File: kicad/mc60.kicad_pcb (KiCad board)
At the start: 2 copper layers, 60 x 70 mm, 107 parts, among them CN1 Conn_GPS, CN2 Conn_GNSS, CN3 SD_CARD, CN4 SIM_Card, CN5 Audio-Jack-4, CN6 5V_IN, J1 B_LS_N, J2 B_VRTC, J3 B_SPKP, J4 B_SPKN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

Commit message: layout WIP
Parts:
- H4: value ON_OFF -> ON<>OFF
- moved G3 57.7 mm to (121.5, 75.0)
- moved D3 18.1 mm to (98.5, 120.0), turned to 0 degrees
- moved R9 14.5 mm to (98.5, 118.0)
- moved R8 13.0 mm to (125.3, 75.8)
- moved Q1 12.9 mm to (123.0, 76.0), turned to 90 degrees
- moved D2 12.8 mm to (127.1, 76.0)
- moved Q2 10.8 mm to (98.5, 115.5), turned to 270 degrees
- moved R14 9.66 mm to (116.8, 107.0), turned to 270 degrees
- moved C1 2.52 mm to (112.0, 88.2), turned to 90 degrees
- moved C17 0.90 mm to (118.2, 106.8), turned to 270 degrees
- moved C16 0.75 mm to (115.2, 106.8), turned to 270 degrees
- moved G2 0.43 mm to (119.8, 123.2)
- moved G1 0.14 mm to (125.5, 119.5)
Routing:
- net /NETLIGHT: track 18.2 -> 33.9 mm
- net /GNSSVCC: track 32.7 -> 17.3 mm, vias 2 -> 0
- net VBAT: track 144.6 -> 141.3 mm
- net /VDD_EXT: track 63.6 -> 60.3 mm
- net GNDD: track 78.6 -> 75.8 mm
- net VDD: track 141.8 -> 143.8 mm
- net GND: track 269.3 -> 271.3 mm, vias 159 -> 161
- net Net-(Q2-Pad3): track 1.25 -> 2.10 mm
- net /SD_DET>: track 42.5 -> 41.9 mm
- net Net-(D3-Pad1): track 1.45 -> 2.02 mm
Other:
- board text added: "CITA STYLE TRSS L | R | G | M"
- board text added: "GND|3V3|GND"
- board text added: "GND|TXD|RXD"
- board text added: "ON<>OFF"
- board text added: "TXD|RNG|DTR|RTS DET|RXD|DCD|CTS"
- board text added: "[-] [+]"

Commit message: layout wip
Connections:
- CN3 pad 1: Net-(CN3-Pad1) -> (no net)
- CN3 pad 2: Net-(CN3-Pad2) -> (no net)
- CN3 pad 8: Net-(CN3-Pad8) -> (no net)
- CN4 pad P6: Net-(CN4-PadP6) -> (no net)
- D1 pad 4: Net-(D1-Pad4) -> (no net)
- D1 pad 5: Net-(D1-Pad5) -> (no net)
- D4 pad 4: Net-(D4-Pad4) -> (no net)
- D4 pad 5: Net-(D4-Pad5) -> (no net)
- U1 pad 10: Net-(U1-Pad10) -> (no net)
- U1 pad 11: Net-(U1-Pad11) -> (no net)
- U1 pad 12: Net-(U1-Pad12) -> (no net)
- U1 pad 13: Net-(U1-Pad13) -> (no net)
- U1 pad 46: Net-(U1-Pad46) -> (no net)
- U1 pad 55: Net-(U1-Pad55) -> (no net)
- U1 pad 56: Net-(U1-Pad56) -> (no net)
- U1 pad 57: Net-(U1-Pad57) -> (no net)
- U1 pad 58: Net-(U1-Pad58) -> (no net)
- U1 pad 59: Net-(U1-Pad59) -> (no net)
- U1 pad 60: Net-(U1-Pad60) -> (no net)
- U1 pad 61: Net-(U1-Pad61) -> (no net)
- U1 pad 62: Net-(U1-Pad62) -> (no net)
- U1 pad 63: Net-(U1-Pad63) -> (no net)
- U1 pad 64: Net-(U1-Pad64) -> (no net)
- U1 pad 65: Net-(U1-Pad65) -> (no net)
- U1 pad 66: Net-(U1-Pad66) -> (no net)
- U1 pad 67: Net-(U1-Pad67) -> (no net)
- U1 pad 68: Net-(U1-Pad68) -> (no net)
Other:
- net class 0.70mm removed
- net class 0.72mm added: clearance 0.2, trace_width 0.69, via_dia 0.8, via_drill 0.4
- net class 0.7mmANT added: clearance 0.128, trace_width 0.7, via_dia 0.7, via_drill 0.4
- net class Default: clearance 0.2 -> 0.128
- rule trace_clearance: 0.2 -> 0.128
- rule trace_min: 0.2 -> 0.1

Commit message: layout WIP
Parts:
- added G2: KiCad, mc60_fp:KiCad-Logo2_6mm_SilkScreen_Mask, F.Cu at (119.8, 123.2)
- G1: footprint mc60_fp:Logo_silk_OSHW_6x6mm -> mc60_fp:Logo_silk_OSHW_6x6mm_mask
- moved G3 6.50 mm to (115.5, 72.5), turned to 45 degrees
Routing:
- net VDD: track 143.8 -> 153.8 mm
- net /2V8_SD: track 36.6 -> 43.9 mm
- net GND: track 271.3 -> 272.8 mm, vias 161 -> 163
- net /RIGHT: track 11.5 -> 10.1 mm
- net /MIC_P: track 44.3 -> 43.4 mm
- added copper zone on F.Cu, net (none)
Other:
- net class Default: clearance 0.128 -> 0.2
- rule trace_clearance: 0.128 -> 0.2
- board text added: "CTIA STYLE TRSS L|R|G|M"
- board text added: "WYOLUM"
- board text removed: "CITA STYLE TRSS L | R | G | M"

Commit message: layout wip
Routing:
- net GND: track 272.8 -> 274.1 mm
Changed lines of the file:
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@@
-(kicad_pcb (version 20171130) (host pcbnew 5.0.0-rc2-dev-unknown-5d71153~64~ubuntu17.10.1)
+(kicad_pcb (version 20171130) (host pcbnew 5.0.0-rc2-dev-unknown-c8a7840~64~ubuntu16.04.1)
   (general
     (thickness 1.6)
     (drawings 25)
-    (tracks 1046)
+    (tracks 1048)
     (zones 0)
     (modules 108)
@@
     (0 F.Cu signal)
     (31 B.Cu signal)
-    (32 B.Adhes user hide)
-    (33 F.Adhes user hide)
+    (32 B.Adhes user)
+    (33 F.Adhes user)
     (34 B.Paste user hide)
     (35 F.Paste user hide)
     (36 B.SilkS user)
     (37 F.SilkS user)
-    (38 B.Mask user hide)
+    (38 B.Mask user)
     (39 F.Mask user)
     (40 Dwgs.User user)
@@
       (effects (font (size 0.8 0.8) (thickness 0.12)) (justify mirror))
     )
-    (fp_text value B_LS_N (at 0 -3.5 -90) (layer B.SilkS)
+    (fp_text value B_LS_N (at 0 -3.5 90) (layer B.SilkS)
       (effects (font (size 0.8 0.8) (thickness 0.12)) (justify mirror))
     )
@@
   (via (at 92.25 112.25) (size 0.7) (drill 0.4) (layers F.Cu B.Cu) (net 1))
   (segment (start 92.25 111.5) (end 92.25 112.25) (width 0.7) (layer F.Cu) (net 1))
+  (segment (start 126.75 108.15) (end 126.6 108.3) (width 0.7) (layer F.Cu) (net 1))
+  (segment (start 126.75 107) (end 126.75 108.15) (width 0.7) (layer F.Cu) (net 1))
   (segment (start 119.15 111.73) (end 120.45 111.73) (width 0.7) (layer F.Cu) (net 2) (status 30))
   (segment (start 125.07 111.73) (end 125.075 111.725) (width 0.7) (layer F.Cu) (net 2) (status 30))

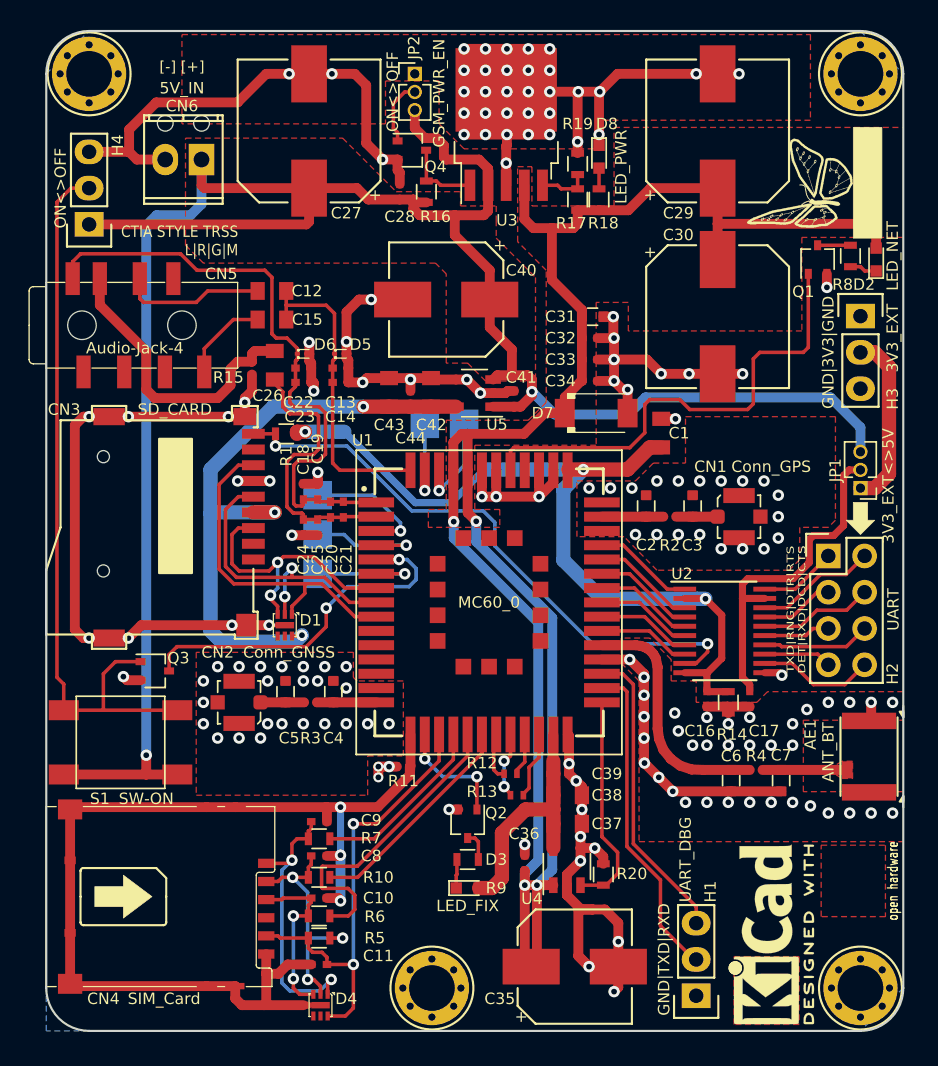
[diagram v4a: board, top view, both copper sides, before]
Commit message: UART header update, added freeite bead on Loudspeaker, added Cap for Switch
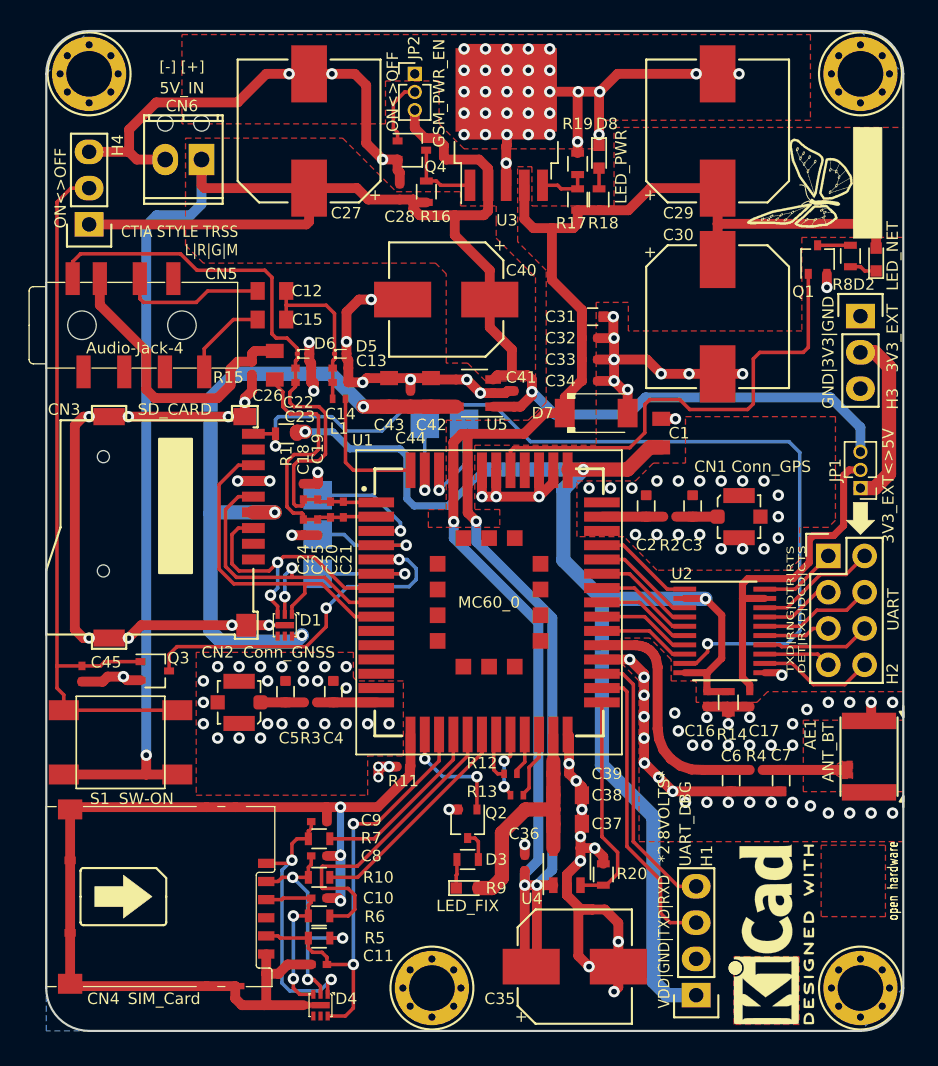
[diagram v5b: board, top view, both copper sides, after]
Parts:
- added C45: 33pF, mc60_fp:C_0402_NoSilk, F.Cu at (71.5, 105.0)
- added L1: 0E, mc60_fp:R_0402_NoSilk, F.Cu at (89.5, 85.8)
- H1: footprint mc60_fp:Pin_Header_Straight_1x03 -> mc60_fp:Pin_Header_Straight_1x04
- moved H1 2.50 mm to (114.5, 127.5)
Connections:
- C12 pad 1: /LOUD_SPKP -> /L_SP
- C13 pad 2: /LOUD_SPKP -> /L_SP
- C14 pad 2: /LOUD_SPKP -> /L_SP
- C15 pad 1: /LOUD_SPKP -> /L_SP
- D5 pad 1: /LOUD_SPKP -> /L_SP
- H1 pad 1: GND -> /VDD_EXT
- H1 pad 2: /DBG_TXD -> GND
- H1 pad 3: /DBG_RXD -> /DBG_TXD
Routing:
- net /VDD_EXT: track 60.3 -> 93.9 mm
- net /SD_DET>: track 41.9 -> 65.4 mm
- net /LOUD_SPKP: track 21.8 -> 9.23 mm
- net /L_SP: track 0.00 -> 11.7 mm
- net /2V8_SD: track 43.9 -> 48.8 mm
- net GND: track 274.1 -> 276.1 mm
- net /DBG_RXD: track 21.0 -> 19.2 mm
- net /DBG_TXD: track 22.7 -> 21.1 mm
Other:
- board text added: "*2.8VOLTS*"
- board text added: "VDD|GND|TXD|RXD"
- board text removed: "GND|TXD|RXD"

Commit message: board layout WIP
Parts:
- removed the G2 at (119.8, 123.2) (x2)
- added G2: KiCad, mc60_fp:KiCad-Logo3_6mm_SilkScreen, F.Cu at (119.8, 123.2)
- G3: footprint mc60_fp:Logo-WL3 -> mc60_fp:logo_wyo3
- S1: footprint mc60_fp:SW_SPST_DTSM -> mc60_fp:SW_SPST_WS_TASV
- moved G3 55.5 mm to (75.2, 110.8), turned to 0 degrees
- moved JP1 10.3 mm to (122.8, 82.2)
- moved C45 4.56 mm to (76.0, 105.8), turned to 270 degrees
- moved S1 4.39 mm to (72.5, 105.8)
- moved D4 2.82 mm to (90.8, 127.0), turned to 270 degrees
- moved Q3 1.69 mm to (78.0, 105.8), turned to 90 degrees
- moved JP2 1.27 mm to (94.8, 64.3)
- moved U2 1.00 mm to (117.5, 102.0)
- moved U3 0.20 mm to (101.0, 70.8)
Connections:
- CN3 pad 1: (no net) -> Net-(CN3-Pad1)
- CN3 pad 2: (no net) -> Net-(CN3-Pad2)
- CN3 pad 8: (no net) -> Net-(CN3-Pad8)
- CN4 pad P6: (no net) -> Net-(CN4-PadP6)
- D1 pad 4: (no net) -> Net-(D1-Pad4)
- D1 pad 5: (no net) -> Net-(D1-Pad5)
- D4 pad 4: (no net) -> Net-(D4-Pad4)
- D4 pad 5: (no net) -> Net-(D4-Pad5)
- SC1 pad 1: (no net) -> GND
- SC2 pad 1: (no net) -> GND
- SC3 pad 1: (no net) -> GND
- SC4 pad 1: (no net) -> GND
- U1 pad 10: (no net) -> Net-(U1-Pad10)
- U1 pad 11: (no net) -> Net-(U1-Pad11)
- U1 pad 12: (no net) -> Net-(U1-Pad12)
- U1 pad 13: (no net) -> Net-(U1-Pad13)
- U1 pad 46: (no net) -> Net-(U1-Pad46)
- U1 pad 55: (no net) -> Net-(U1-Pad55)
- U1 pad 56: (no net) -> Net-(U1-Pad56)
- U1 pad 57: (no net) -> Net-(U1-Pad57)
- U1 pad 58: (no net) -> Net-(U1-Pad58)
- U1 pad 59: (no net) -> Net-(U1-Pad59)
- U1 pad 60: (no net) -> Net-(U1-Pad60)
- U1 pad 61: (no net) -> Net-(U1-Pad61)
- U1 pad 62: (no net) -> Net-(U1-Pad62)
- U1 pad 63: (no net) -> Net-(U1-Pad63)
- U1 pad 64: (no net) -> Net-(U1-Pad64)
- U1 pad 65: (no net) -> Net-(U1-Pad65)
- U1 pad 66: (no net) -> Net-(U1-Pad66)
- U1 pad 67: (no net) -> Net-(U1-Pad67)
- U1 pad 68: (no net) -> Net-(U1-Pad68)
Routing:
- net GND: track 276.1 -> 337.2 mm, vias 163 -> 236
- net VDD: track 153.8 -> 140.6 mm
- net /VCCB: track 23.8 -> 33.4 mm
- net /3V3_EXT: track 12.3 -> 3.67 mm
- net /RST: track 52.3 -> 43.9 mm
- net /SD_DET>: track 65.4 -> 69.9 mm
- net GNDD: track 75.8 -> 79.9 mm
- net /SIM1_VDD: track 32.2 -> 29.5 mm
- net /SIMRST: track 12.2 -> 14.9 mm
- net /SIMDAT: track 17.2 -> 19.3 mm
- net /TXD>: track 6.47 -> 7.89 mm
- net /VDD_EXT: track 93.9 -> 95.3 mm
- net /RING>: track 6.76 -> 7.76 mm
- net /RING: track 4.66 -> 3.66 mm
- net /SD_DET: track 8.18 -> 7.18 mm
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- removed copper zone on F.Cu, net (none)
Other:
- outline, holes or cut-outs redrawn
- board text added: "DET|RXD|DCD|CTS"
- board text added: "TXD|RNG|DTR|RTS"
- board text removed: "TXD|RNG|DTR|RTS DET|RXD|DCD|CTS"

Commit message: board layout, WiP
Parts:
- G1, G2: moved to B.Cu
- moved G3 49.9 mm to (124.0, 121.5), turned to 90 degrees
- moved G1 45.0 mm to (80.5, 117.7), turned to 270 degrees
- moved G2 44.8 mm to (75.0, 121.0), turned to 270 degrees
- moved C35 0.50 mm to (106.0, 125.0)
- moved S1 0.10 mm to (72.6, 105.8)
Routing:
- net GND: track 337.2 -> 420.4 mm, vias 236 -> 358
- net VDD: track 140.6 -> 142.1 mm
- net /RST: track 43.9 -> 44.1 mm, vias 0 -> 1
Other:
- board text added: "CTS|DCD|RXD|DET"
- board text added: "L|R|G|M CTIA STYLE TRSS"
- board text added: "RTS|DTR|RNG|TXD"
- board text added: "RXD|TXD|GND|VDD"
- board text removed: "CTIA STYLE TRSS L|R|G|M"
- board text removed: "DET|RXD|DCD|CTS"
- board text removed: "TXD|RNG|DTR|RTS"
- board text removed: "VDD|GND|TXD|RXD"

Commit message: board layout, WiP
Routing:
- net GND: track 420.4 -> 422.0 mm
